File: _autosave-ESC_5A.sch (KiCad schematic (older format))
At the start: 26 parts, among them IC1 EEPROM, IC2 3.3V Reg, IC3 5V_Reg, IC4 ATSAMD21E17D-AUT, J1 USBc, J2 5V_PWR

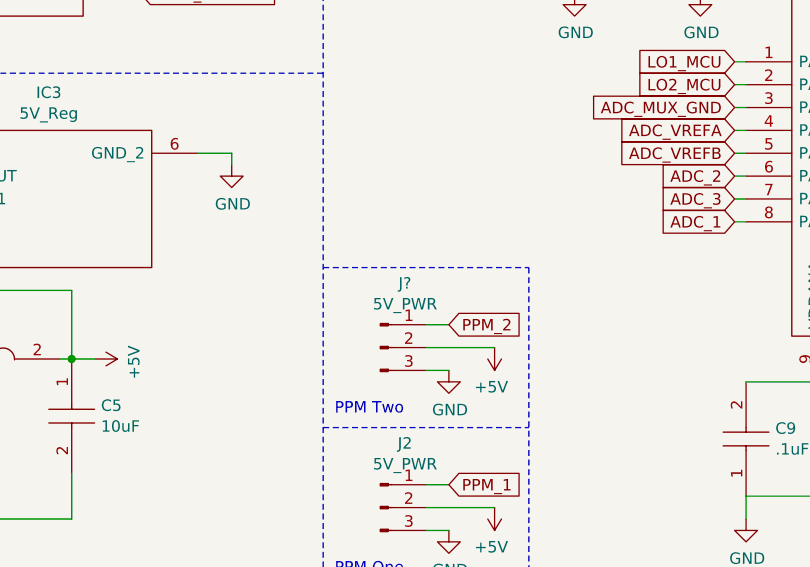
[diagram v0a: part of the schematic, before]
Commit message: Checking on layout of driver VDD
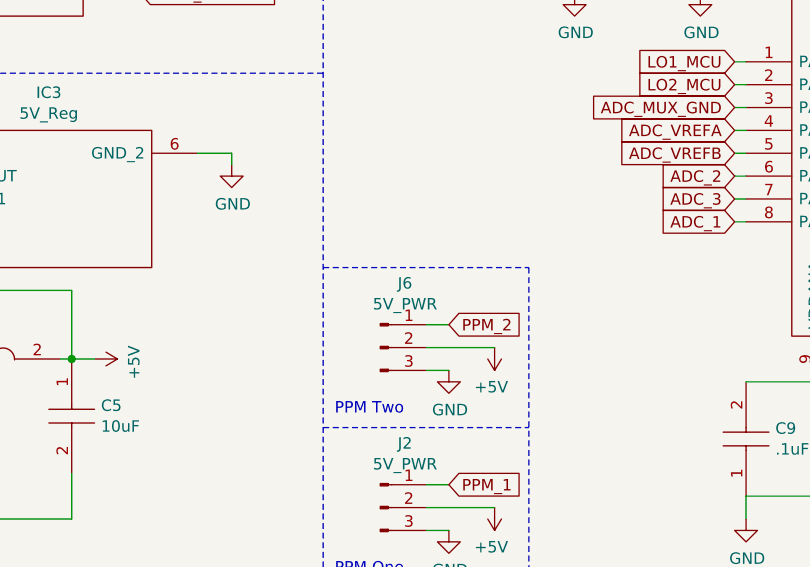
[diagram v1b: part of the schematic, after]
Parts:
- gave numbers to parts that had none: 1
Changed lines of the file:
@@
 $EndComp
 $Comp
-L Connector:Conn_01x03_Male J?
+L Connector:Conn_01x03_Male J6
 U 1 1 60FBA964
 P 7150 5400
-F 0 "J?" H 7258 5681 50  0000 C CNN
+F 0 "J6" H 7258 5681 50  0000 C CNN
 F 1 "5V_PWR" H 7258 5590 50  0000 C CNN
 F 2 "Connector_PinHeader_2.54mm:PinHeader_1x03_P2.54mm_Vertical" H 7150 5400 50  0001 C CNN
@@
 	7350 5500 7450 5500
 $Comp
-L power:GND #PWR?
+L power:GND #PWR0104
 U 1 1 60FBA96B
 P 7450 5500
-F 0 "#PWR?" H 7450 5250 50  0001 C CNN
+F 0 "#PWR0104" H 7450 5250 50  0001 C CNN
 F 1 "GND" H 7455 5327 50  0000 C CNN
 F 2 "" H 7450 5500 50  0001 C CNN
@@
 $EndComp
 $Comp
-L power:+5V #PWR?
+L power:+5V #PWR0105
 U 1 1 60FBA972
 P 7650 5400
-F 0 "#PWR?" H 7650 5250 50  0001 C CNN
+F 0 "#PWR0105" H 7650 5250 50  0001 C CNN
 F 1 "+5V" H 7665 5573 50  0000 C CNN
 F 2 "" H 7650 5400 50  0001 C CNN
